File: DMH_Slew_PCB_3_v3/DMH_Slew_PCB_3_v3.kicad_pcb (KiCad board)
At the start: 2 copper layers, 50 x 100 mm, 63 parts, among them J11 Conn_02x03_Top_Bottom, J12 Conn_02x06_Top_Bottom, J13 Conn_02x03_Top_Bottom, Q1 BC548, Q2 BC548, Q3 BC558, Q4 BC558, Q5 BC548, Q6 BC548, U1 TL074, U2 TL074

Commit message: PCB 3 comp placement done
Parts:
- Q1, Q2, Q3, Q4, Q5, Q6: footprint Package_TO_SOT_THT:TO-92_Inline -> Package_TO_SOT_THT:TO-92L_Inline_Wide
- moved R21 93.9 mm to (60.0, 122.2)
- moved R20 63.9 mm to (60.0, 117.3)
- moved R19 63.5 mm to (60.0, 112.4)
- moved R18 63.2 mm to (60.0, 107.4)
- moved R17 62.8 mm to (60.0, 102.5)
- moved R16 62.5 mm to (60.0, 97.6)
- moved R15 62.2 mm to (60.0, 92.7)
- moved R14 61.9 mm to (60.0, 87.7)
- moved R13 61.6 mm to (60.0, 82.8)
- moved R12 61.3 mm to (60.0, 77.8)
- moved R26 58.4 mm to (90.0, 122.2)
- moved R25 57.7 mm to (90.0, 117.3)
- moved R24 57.1 mm to (90.0, 112.4)
- moved R23 56.4 mm to (90.0, 107.4)
- moved R22 55.8 mm to (90.0, 102.5)
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
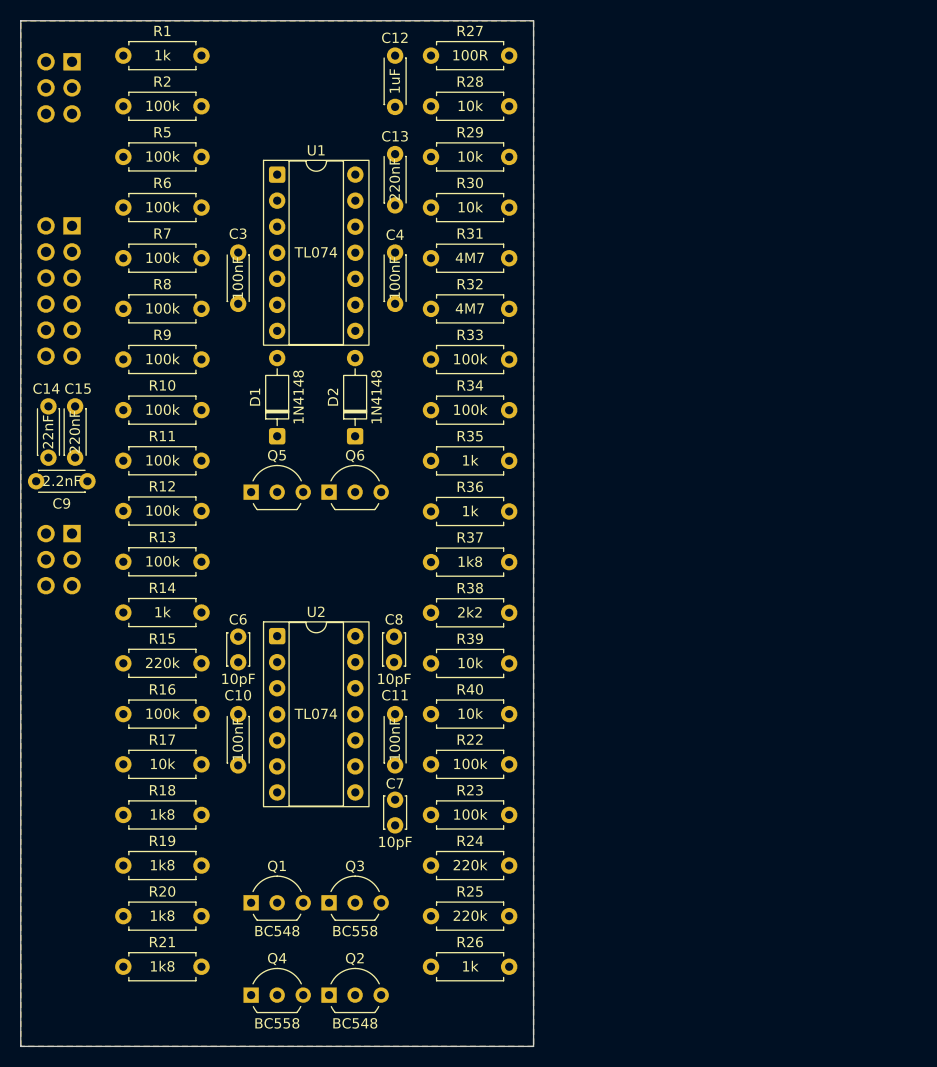
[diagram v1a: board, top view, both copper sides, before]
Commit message: PCB 3 routing in progress
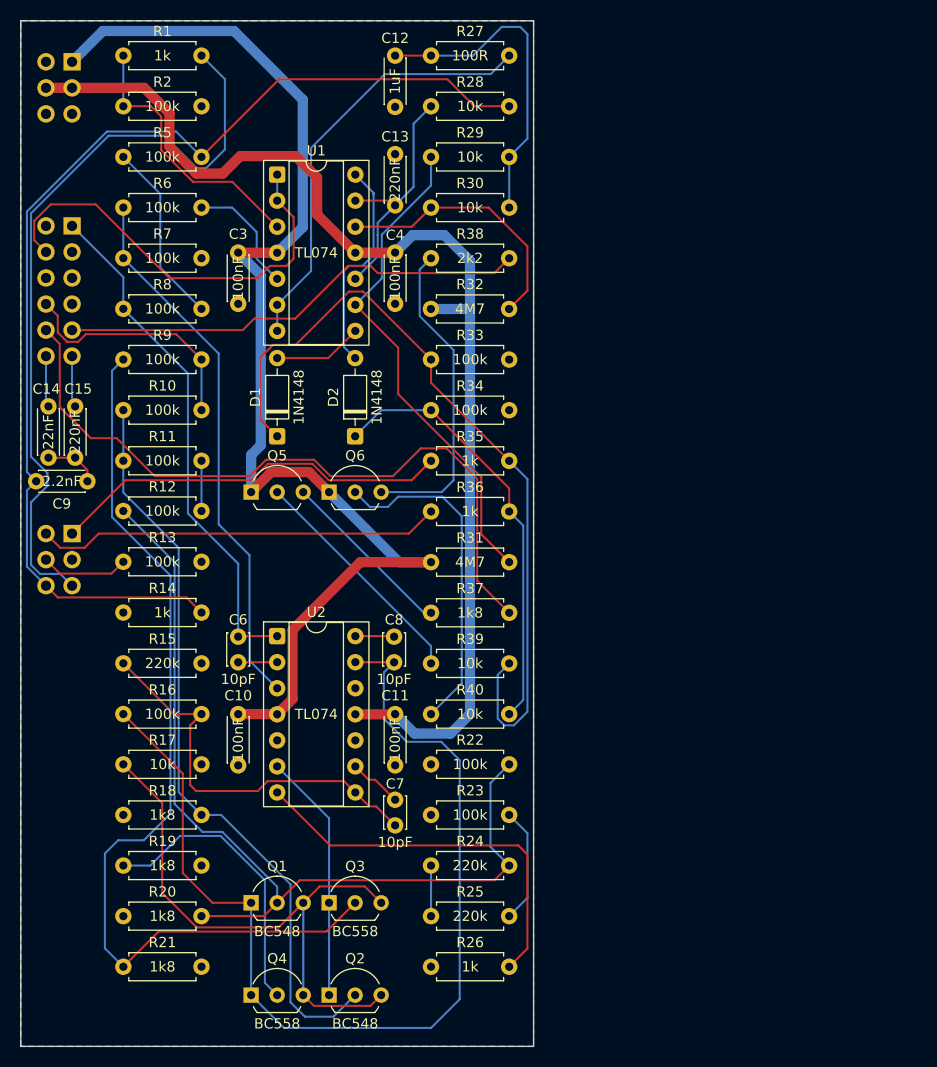
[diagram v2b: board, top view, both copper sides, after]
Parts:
- moved R38 34.6 mm to (90.0, 53.2)
- moved R31 29.6 mm to (90.0, 82.8)
- moved R32 7.61 mm to (97.6, 58.1), turned to 180 degrees
- moved R37 4.94 mm to (90.0, 87.7)
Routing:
- net +12V: track 0.00 -> 121.8 mm
- net -12V: track 0.00 -> 116.0 mm
- net A_Out_Jack_S: track 0.00 -> 109.7 mm
- net /Core Circuit A/A_Comp_F: track 0.00 -> 103.4 mm
- net Net-(Q1-C): track 0.00 -> 99.7 mm
- net /Core Circuit A/A_Comp_R: track 0.00 -> 89.0 mm
- net Net-(D1-K): track 0.00 -> 78.2 mm
- net A_CV_In_Jack_S: track 0.00 -> 74.6 mm
- net /Core Circuit A/A_Comp_-R: track 0.00 -> 73.4 mm
- net A_F_LED_S: track 0.00 -> 69.6 mm
- net Net-(Q1-E): track 0.00 -> 56.6 mm
- net Net-(U2A-+): track 0.00 -> 53.1 mm
- net A_Diff_Amp_S: track 0.00 -> 50.6 mm
- net Net-(U1C--): track 0.00 -> 48.8 mm
- net A_R_LED_S: track 0.00 -> 46.1 mm
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
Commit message: Submodule routing done
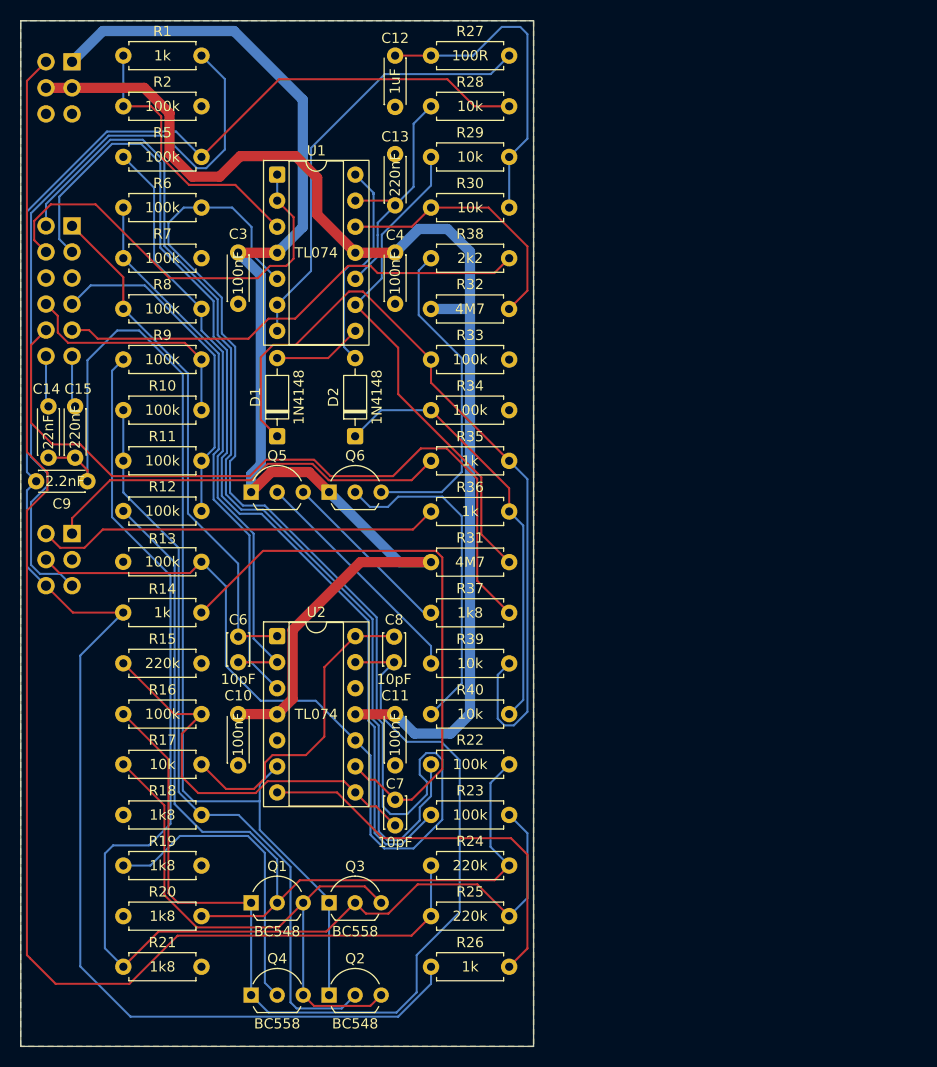
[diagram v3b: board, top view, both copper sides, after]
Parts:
- moved R13 7.61 mm to (67.6, 82.8), turned to 180 degrees
- moved R14 7.61 mm to (67.6, 87.7), turned to 180 degrees
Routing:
- net A_Input_Jack_S: track 20.4 -> 162.0 mm
- net +10V_A: track 4.93 -> 137.8 mm
- net A_Rise_CV_S: track 0.00 -> 103.9 mm
- net A_Fall_CV_S: track 0.00 -> 101.5 mm
- net Net-(Q2-C): track 29.8 -> 103.8 mm
- net A_Out_Jack_S: track 109.7 -> 177.6 mm
- net Net-(U2C--): track 5.23 -> 58.0 mm
- net Net-(U2A--): track 21.8 -> 59.7 mm
- net A_LinLog_Sw_p5_S: track 4.90 -> 33.2 mm
- net Net-(C8-Pad2): track 3.80 -> 30.8 mm
- net /Core Circuit A/A_Comp_F: track 103.4 -> 121.9 mm
- net A_F_LED_S: track 69.6 -> 73.3 mm
- net Net-(Q1-C): track 99.7 -> 97.8 mm
- net -12V: track 116.0 -> 117.6 mm
- net /Core Circuit A/A_Comp_R: track 89.0 -> 90.5 mm
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
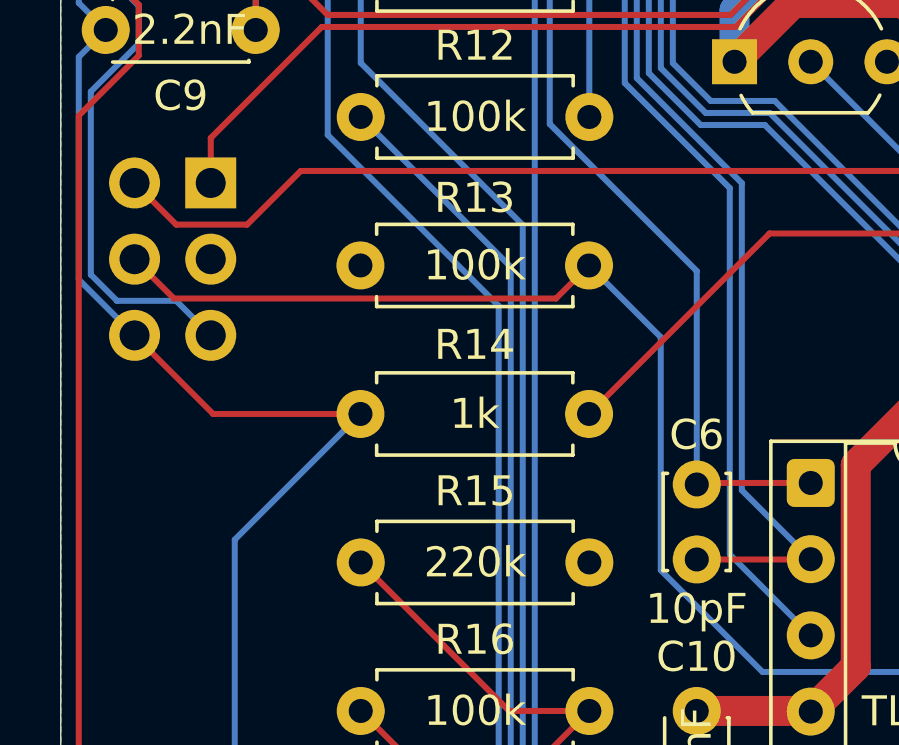
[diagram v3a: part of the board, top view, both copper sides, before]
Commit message: Exposed loopback resistor to submodule connector
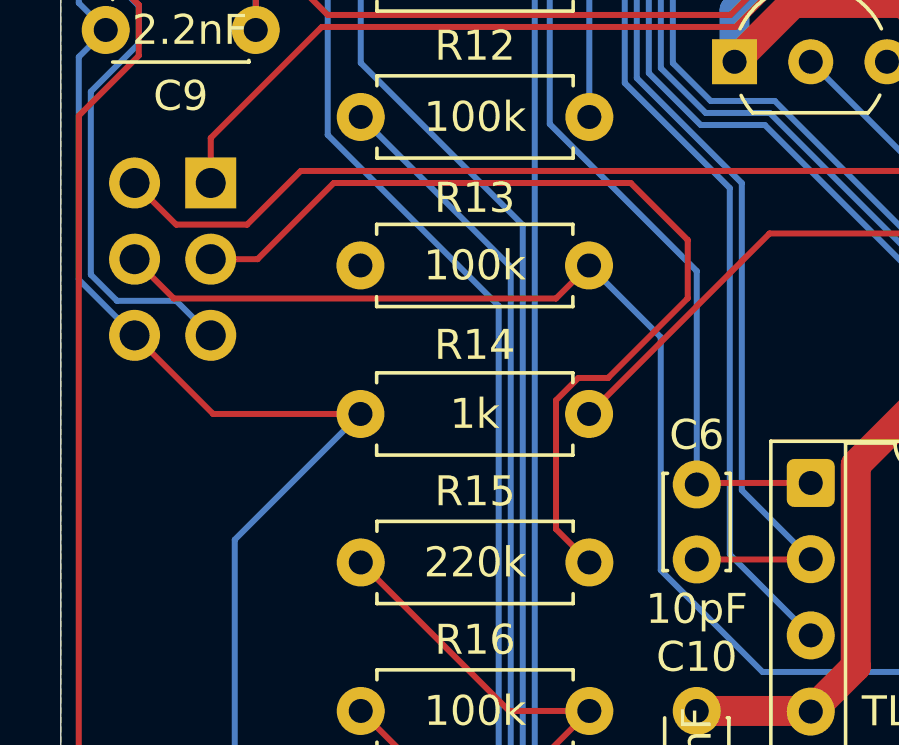
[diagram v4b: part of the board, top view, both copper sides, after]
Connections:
- J13 pad 3: GND -> A_Loopback_S
- R15 pad 2: GND -> A_Loopback_S
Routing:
- net A_Loopback_S: track 0.00 -> 31.3 mm
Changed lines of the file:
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@@
 	(net 45 "Net-(U1C--)")
 	(net 46 "Net-(U1D-+)")
+	(net 47 "A_Loopback_S")
 	(footprint "Resistor_THT:R_Axial_DIN0207_L6.3mm_D2.5mm_P7.62mm_Horizontal"
 		(layer "F.Cu")
@@
 			(layers "*.Cu" "*.Mask")
 			(remove_unused_layers no)
-			(net 1 "GND")
+			(net 47 "A_Loopback_S")
 			(pintype "passive")
 		)
@@
 			(layers "*.Cu" "*.Mask")
 			(remove_unused_layers no)
-			(net 1 "GND")
+			(net 47 "A_Loopback_S")
 			(pinfunction "Pin_3")
 			(pintype "passive")
@@
 		(net 46)
 	)
+	(segment
+		(start 69.001 80.001)
+		(end 70.9 81.9)
+		(width 0.2)
+		(layer "F.Cu")
+		(net 47)
+	)
+	(segment
+		(start 59.1 80.001)
+		(end 69.001 80.001)
+		(width 0.2)
+		(layer "F.Cu")
+		(net 47)
+	)
+	(segment
+		(start 67.25295 86.5)
+		(end 66.509 87.24395)
+		(width 0.2)
+		(layer "F.Cu")
+		(net 47)
+	)
+	(segment
+		(start 66.509 87.24395)
+		(end 66.509 91.539)
+		(width 0.2)
+		(layer "F.Cu")
+		(net 47)
+	)
+	(segment
+		(start 70.9 83.8429)
+		(end 68.2429 86.5)
+		(width 0.2)
+		(layer "F.Cu")
+		(net 47)
+	)
+	(segment
+		(start 68.2429 86.5)
+		(end 67.25295 86.5)
+		(width 0.2)
+		(layer "F.Cu")
+		(net 47)
+	)
+	(segment
+		(start 70.9 81.9)
+		(end 70.9 83.8429)
+		(width 0.2)
+		(layer "F.Cu")
+		(net 47)
+	)
+	(segment
+		(start 56.561 82.54)
+		(end 59.1 80.001)
+		(width 0.2)
+		(layer "F.Cu")
+		(net 47)
+	)
+	(segment
+		(start 55 82.54)
+		(end 56.561 82.54)
+		(width 0.2)
+		(layer "F.Cu")
+		(net 47)
+	)
+	(segment
+		(start 66.509 91.539)
+		(end 67.62 92.65)
+		(width 0.2)
+		(layer "F.Cu")
+		(net 47)
+	)
 	(zone

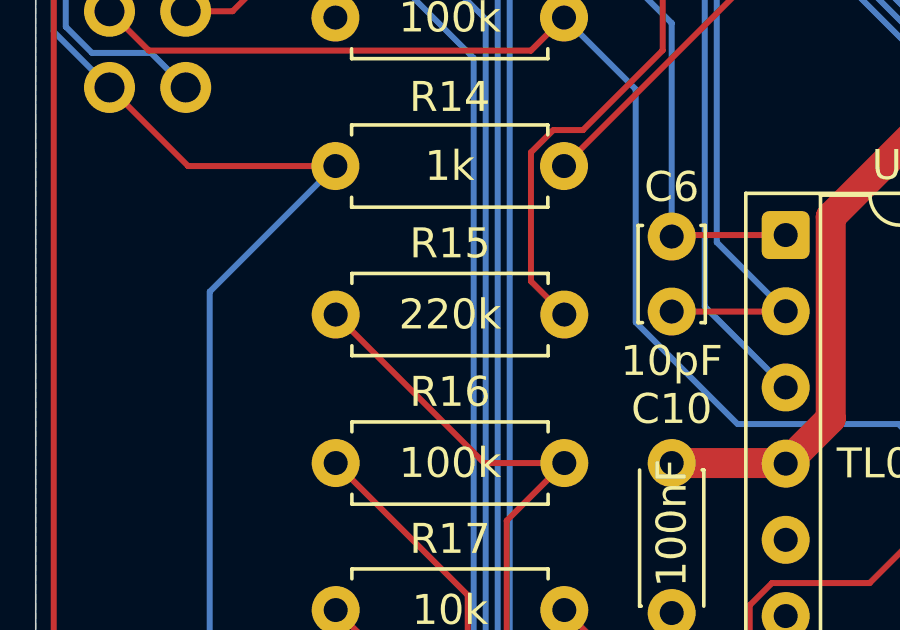
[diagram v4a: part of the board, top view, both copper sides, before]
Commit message: Changed loopback resistor to 82k
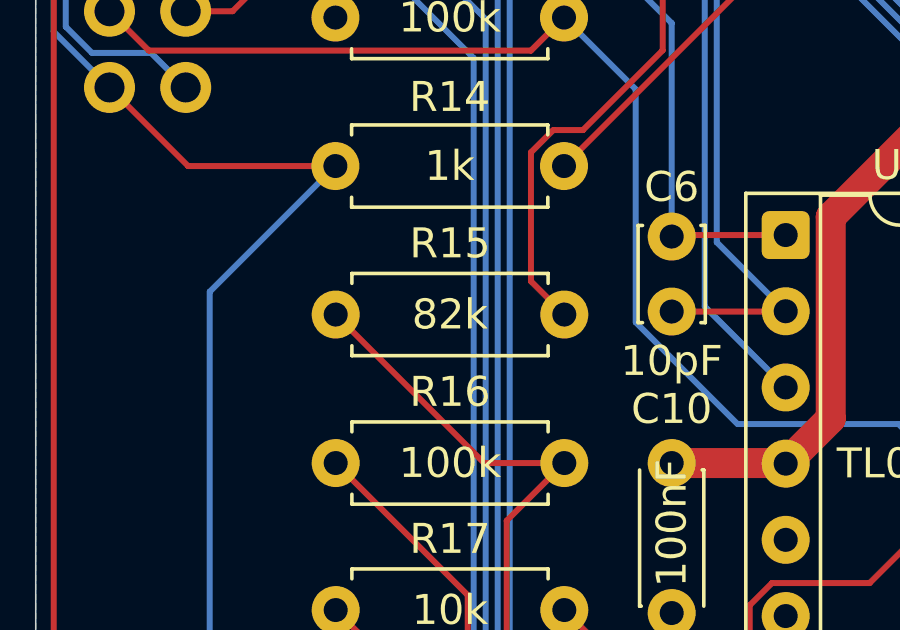
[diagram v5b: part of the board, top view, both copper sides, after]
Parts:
- R15: value 220k -> 82k
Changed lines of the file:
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@@
 			)
 		)
-		(property "Value" "220k"
+		(property "Value" "82k"
 			(at 3.81 0 0)
 			(layer "F.SilkS")

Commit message: Generated Gerbers
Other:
- board text added: "Mk1.0 - March 2026"
- board text removed: "Mk1.0 - Month Year"
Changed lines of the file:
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@@
 			(plot_on_all_layers_selection 0x00000000_00000000_00000000_00000000)
 			(disableapertmacros no)
-			(usegerberextensions no)
+			(usegerberextensions yes)
 			(usegerberattributes yes)
 			(usegerberadvancedattributes yes)
@@
 			(sketchdnponfab yes)
 			(crossoutdnponfab yes)
-			(subtractmaskfromsilk no)
+			(subtractmaskfromsilk yes)
 			(outputformat 1)
 			(mirror no)
-			(drillshape 1)
+			(drillshape 0)
 			(scaleselection 1)
-			(outputdirectory "")
+			(outputdirectory "Gerbers/")
 		)
 	)
@@
 		(layer "Edge.Cuts")
 	)
-	(gr_text "Mk1.0 - Month Year"
+	(gr_text "Mk1.0 - March 2026"
 		(at 59.75 128.75 0)
 		(layer "B.SilkS")

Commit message: Adjustments after prototyping
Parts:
- R37: value 1k8 -> 2k2
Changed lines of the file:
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@@
 		(property "Value" "BC548"
 			(at 2.54 2.79 0)
-			(layer "F.Fab")
+			(layer "F.SilkS")
 			(effects
 				(font
@@
 			)
 		)
-		(property "Value" "1k8"
+		(property "Value" "2k2"
 			(at 3.81 0 0)
 			(layer "F.SilkS")
@@
 		)
 		(property "Value" "TL074"
-			(at 3.81 7.615 0)
+			(at 3.81 7.615 90)
 			(layer "F.SilkS")
 			(effects
@@
 		(property "Value" "BC548"
 			(at 2.54 2.79 0)
-			(layer "F.Fab")
+			(layer "F.SilkS")
 			(effects
 				(font
@@
 		)
 		(property "Value" "TL074"
-			(at 3.81 7.615 0)
+			(at 3.81 7.615 90)
 			(layer "F.SilkS")
 			(effects

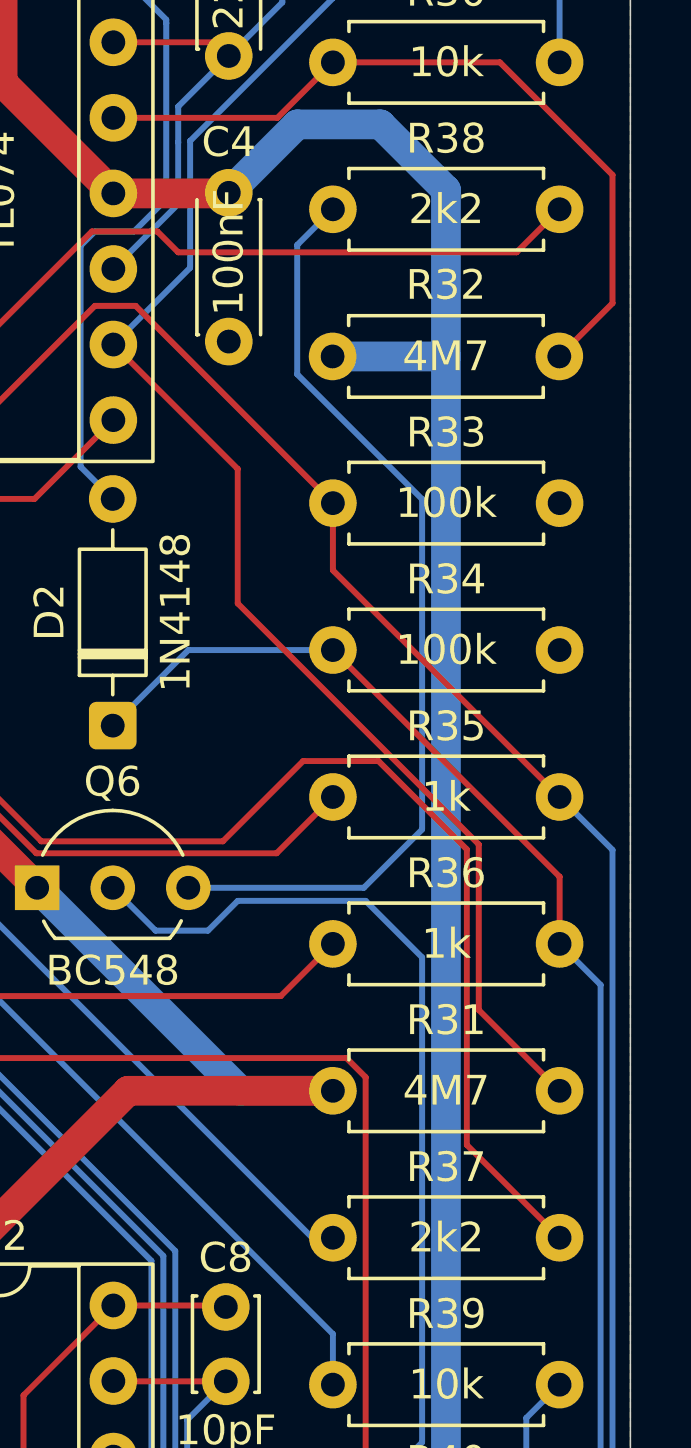
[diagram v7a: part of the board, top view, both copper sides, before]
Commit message: Corrected PCB 2 switch positions
and Regenerated Gerbers
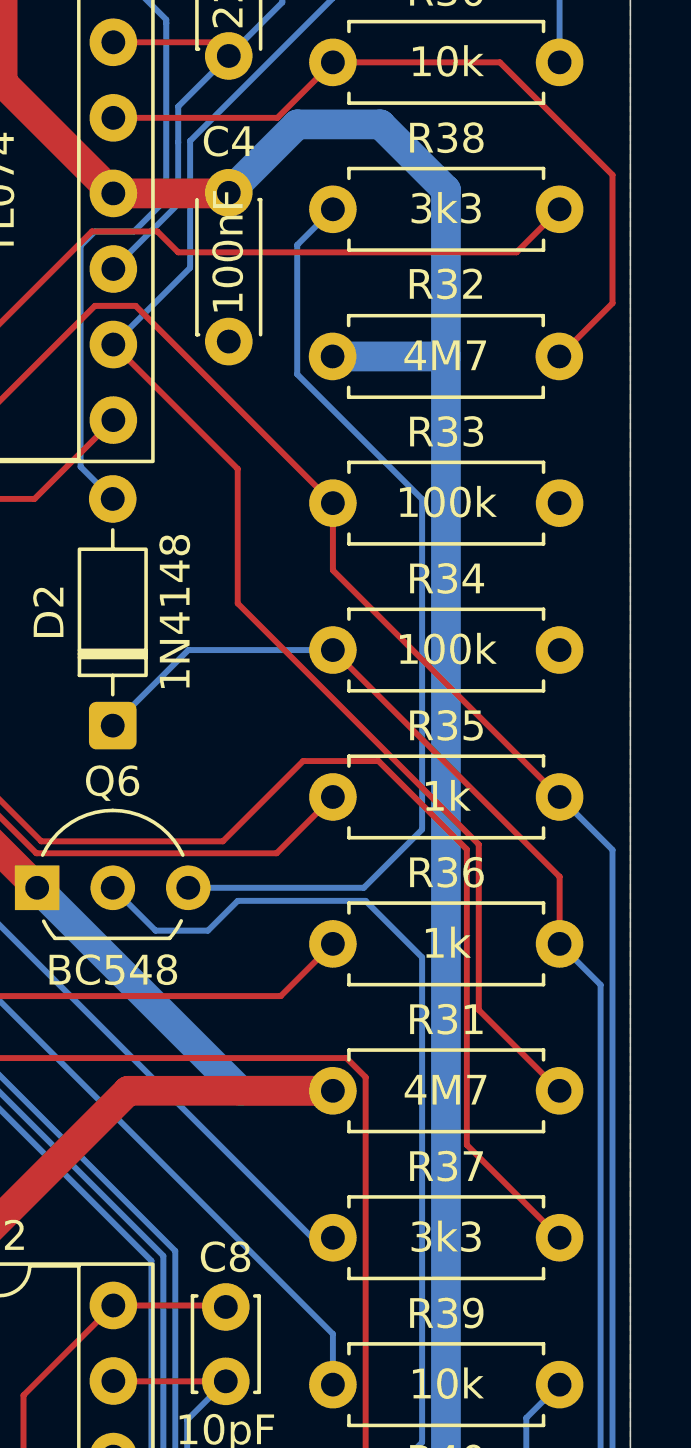
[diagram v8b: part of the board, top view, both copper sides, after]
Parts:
- R37, R38: value 2k2 -> 3k3
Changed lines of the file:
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@@
 			)
 		)
-		(property "Value" "2k2"
+		(property "Value" "3k3"
 			(at 3.81 0 0)
 			(layer "F.SilkS")
@@
 			)
 		)
-		(property "Value" "2k2"
+		(property "Value" "3k3"
 			(at 3.81 0 0)
 			(layer "F.SilkS")
